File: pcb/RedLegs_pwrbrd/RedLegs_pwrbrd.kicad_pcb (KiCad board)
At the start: 2 copper layers, 25 parts, among them J1 Conn_01x02, J10 Conn_01x02, J11 Conn_01x02, J12 Conn_01x02, J2 Conn_01x02, J3 Conn_01x02, J4 Conn_01x02, J5 Conn_01x02, J6 Conn_01x02, J7 Conn_01x02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

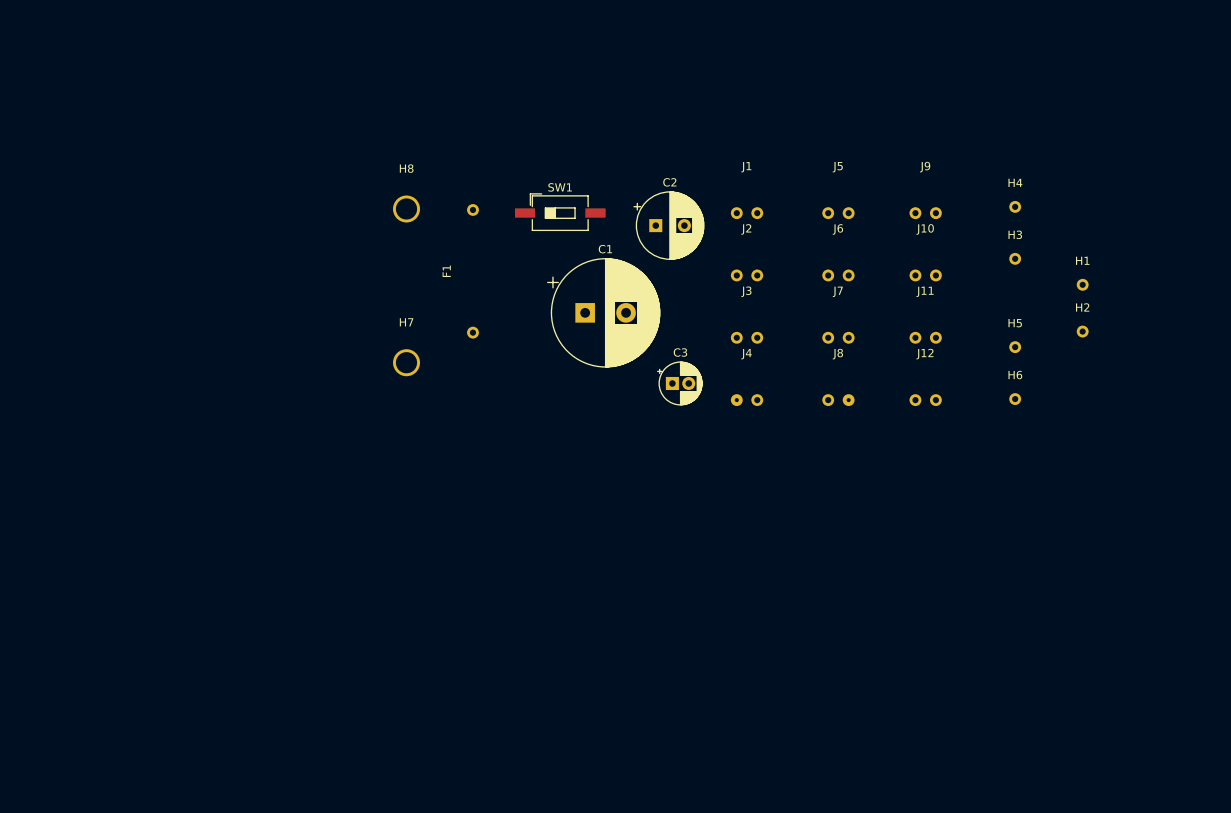
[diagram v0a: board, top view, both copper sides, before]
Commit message: Fixed power schematic, working on pcb
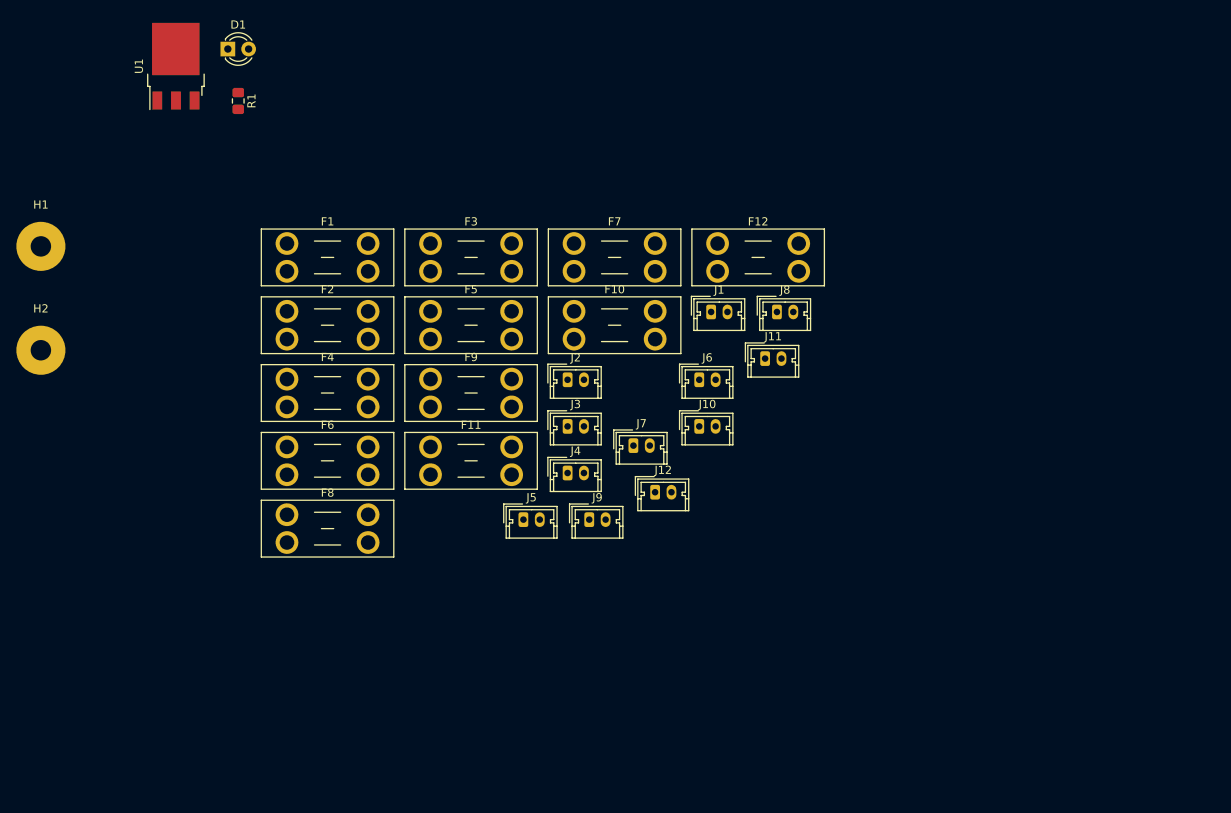
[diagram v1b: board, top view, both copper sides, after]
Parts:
- removed C1: 1000 uf, Capacitor_THT:CP_Radial_D13.0mm_P5.00mm
- removed C2: 100 uf, Capacitor_THT:CP_Radial_D8.0mm_P3.50mm
- removed C3: 10 uf, Capacitor_THT:CP_Radial_D5.0mm_P2.00mm
- removed H3, H4, H5, H6: MountingHole_Pad, MountingHole:MountingHole_2.2mm_M2_DIN965_Pad
- removed H7, H8: MountingHole_Pad, RedLegs_pwrbrd:RedLegsPwrBrdMountingHole
- removed SW1: SW_DIP_x01, Button_Switch_SMD:SW_DIP_SPSTx01_Slide_6.7x4.1mm_W8.61mm_P2.54mm_LowProfile
- added D1: LED, LED_THT:LED_D3.0mm, F.Cu at (71.1, 47.0)
- added F10: Fuse, Fuse:Fuseholder_Blade_Mini_Keystone_3568, F.Cu at (113.5, 79.1)
- added F11: Fuse, Fuse:Fuseholder_Blade_Mini_Keystone_3568, F.Cu at (95.9, 95.6)
- added F12: Fuse, Fuse:Fuseholder_Blade_Mini_Keystone_3568, F.Cu at (131.0, 70.8)
- added F2: Fuse, Fuse:Fuseholder_Blade_Mini_Keystone_3568, F.Cu at (78.3, 79.1)
- added F3: Fuse, Fuse:Fuseholder_Blade_Mini_Keystone_3568, F.Cu at (95.9, 70.8)
- added F4: Fuse, Fuse:Fuseholder_Blade_Mini_Keystone_3568, F.Cu at (78.3, 87.3)
- added F5: Fuse, Fuse:Fuseholder_Blade_Mini_Keystone_3568, F.Cu at (95.9, 79.1)
- added F6: Fuse, Fuse:Fuseholder_Blade_Mini_Keystone_3568, F.Cu at (78.3, 95.6)
- added F7: Fuse, Fuse:Fuseholder_Blade_Mini_Keystone_3568, F.Cu at (113.5, 70.8)
- added F8: Fuse, Fuse:Fuseholder_Blade_Mini_Keystone_3568, F.Cu at (78.3, 103.9)
- added F9: Fuse, Fuse:Fuseholder_Blade_Mini_Keystone_3568, F.Cu at (95.9, 87.3)
- added R1: 330, Resistor_SMD:R_0805_2012Metric_Pad1.15x1.40mm_HandSolder, F.Cu at (72.4, 53.3)
- added U1: L7805, Package_TO_SOT_SMD:TO-252-3_TabPin2, F.Cu at (64.8, 49.1)
- F1: value 30 Amps -> Fuse; footprint RedLegs_pwrbrd:RedLegsPwrBrdFuse -> Fuse:Fuseholder_Blade_Mini_Keystone_3568
- H1: value MountingHole_Pad -> Battery_Positive; footprint MountingHole:MountingHole_2.2mm_M2_DIN965_Pad -> Connector_Wire:SolderWirePad_1x01_Drill2.5mm
- H2: value MountingHole_Pad -> Battery_Ground; footprint MountingHole:MountingHole_2.2mm_M2_DIN965_Pad -> Connector_Wire:SolderWirePad_1x01_Drill2.5mm
- J1, J10, J11, J12, J2, J3, J4, J5, J6, J7, J8, J9: footprint RedLegs_pwrbrd:RedLegsPwrBrdConnector -> Connector_Molex:Molex_Micro-Latch_53253-0270_1x02_P2.00mm_Vertical
- moved H1 127.5 mm to (48.3, 71.1)
- moved H2 127.4 mm to (48.3, 83.8)
- moved J9 55.7 mm to (115.3, 104.5)
- moved J5 53.8 mm to (107.3, 104.5)
- moved J12 35.0 mm to (123.4, 101.2)
- moved J10 33.3 mm to (128.8, 93.1)
- moved J7 28.3 mm to (120.7, 95.5)
- moved J2 25.4 mm to (112.7, 87.4)
- moved J3 24.5 mm to (112.7, 93.1)
- moved J4 23.7 mm to (112.7, 98.8)
- moved F1 23.0 mm to (78.3, 70.8), turned to 0 degrees
- moved J6 21.3 mm to (128.8, 87.4)
- moved J11 19.8 mm to (136.8, 84.8)
- moved J8 13.1 mm to (138.3, 79.1)
- moved J1 12.9 mm to (130.2, 79.1)
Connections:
- net Net-(C1-Pad2) renamed GND
- F1 pad 2: Net-(F1-Pad2) -> +BATT
- H1 pad 1: Net-(C1-Pad1) -> +BATT
- J1 pad 1: Net-(C1-Pad1) -> Net-(F1-Pad1)
- J10 pad 1: Net-(C1-Pad1) -> Net-(F10-Pad1)
- J11 pad 1: Net-(C1-Pad1) -> Net-(F11-Pad1)
- J12 pad 1: Net-(C1-Pad1) -> Net-(F12-Pad1)
- J2 pad 1: Net-(C1-Pad1) -> Net-(F2-Pad1)
- J3 pad 1: Net-(C1-Pad1) -> Net-(F3-Pad1)
- J4 pad 1: Net-(C1-Pad1) -> Net-(F4-Pad1)
- J5 pad 1: Net-(C1-Pad1) -> Net-(F5-Pad1)
- J6 pad 1: Net-(C1-Pad1) -> Net-(F6-Pad1)
- J7 pad 1: Net-(C1-Pad1) -> Net-(F7-Pad1)
- J8 pad 1: Net-(C1-Pad1) -> Net-(F8-Pad1)
- J9 pad 1: Net-(C1-Pad1) -> Net-(F9-Pad1)

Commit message: Finish placement, added master fuse
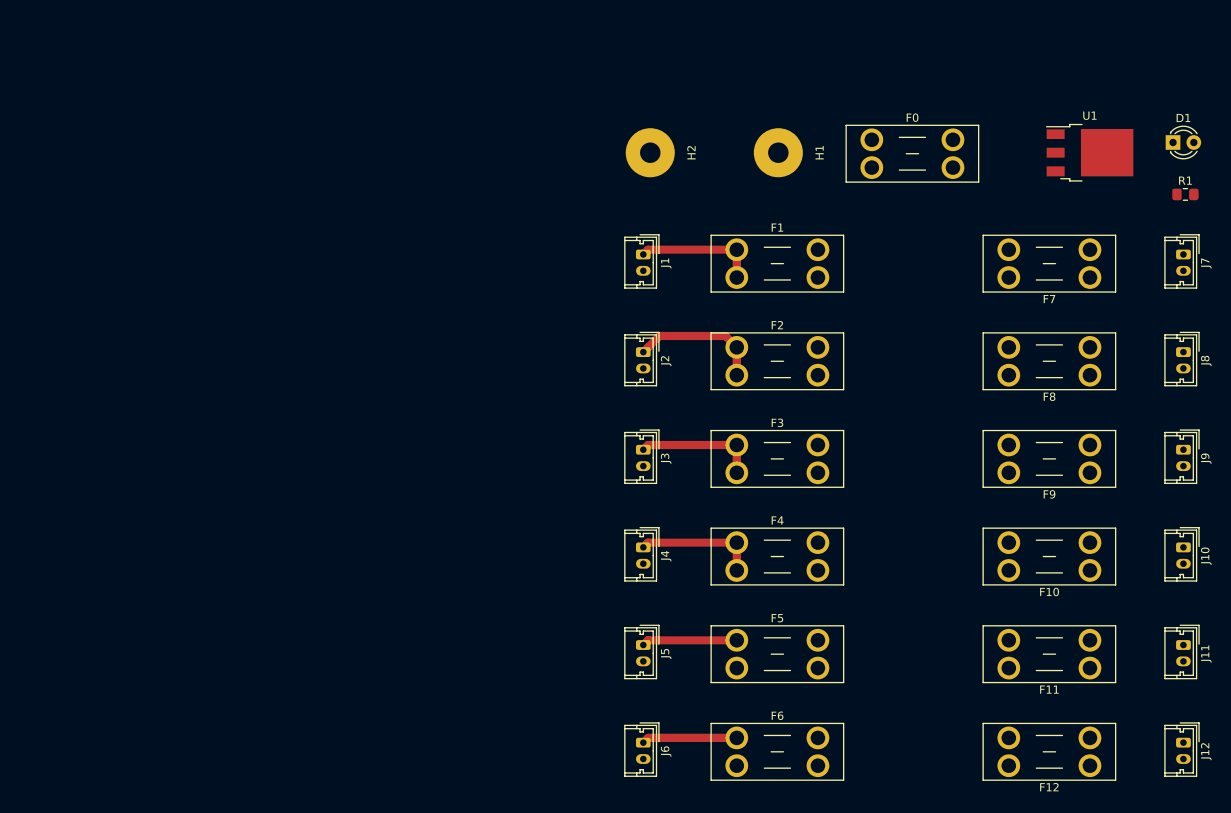
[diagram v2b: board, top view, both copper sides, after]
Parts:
- added F0: Fuse, Fuse:Fuseholder_Blade_Mini_Keystone_3568, F.Cu at (149.9, 58.1)
- moved R1 116.4 mm to (188.2, 64.8), turned to 0 degrees
- moved D1 116.1 mm to (186.7, 58.4)
- moved U1 112.3 mm to (176.5, 59.7), turned to 0 degrees
- moved F8 99.7 mm to (176.5, 86.9), turned to 180 degrees
- moved H1 90.9 mm to (138.4, 59.7), turned to 270 degrees
- moved F11 85.0 mm to (176.5, 122.7), turned to 180 degrees
- moved F9 81.4 mm to (176.5, 98.8), turned to 180 degrees
- moved F12 78.4 mm to (176.5, 134.6), turned to 180 degrees
- moved H2 78.3 mm to (122.8, 59.7), turned to 270 degrees
- moved J9 73.2 mm to (188.0, 96.0), turned to 270 degrees
- moved J12 71.5 mm to (188.0, 131.8), turned to 270 degrees
- moved J7 71.2 mm to (188.0, 72.1), turned to 270 degrees
- moved F10 70.6 mm to (176.5, 110.7), turned to 180 degrees
- moved F6 65.5 mm to (133.3, 131.2)
- moved F7 63.2 mm to (176.5, 74.9), turned to 180 degrees
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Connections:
- F1 pad 2: +BATT -> VCC
- F10 pad 2: +BATT -> VCC
- F11 pad 2: +BATT -> VCC
- F12 pad 2: +BATT -> VCC
- F2 pad 2: +BATT -> VCC
- F3 pad 2: +BATT -> VCC
- F4 pad 2: +BATT -> VCC
- F5 pad 2: +BATT -> VCC
- F6 pad 2: +BATT -> VCC
- F7 pad 2: +BATT -> VCC
- F8 pad 2: +BATT -> VCC
- F9 pad 2: +BATT -> VCC
- U1 pad 1: +BATT -> VCC
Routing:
- net Net-(F2-Pad1): track 0.00 -> 16.2 mm
- net Net-(F4-Pad1): track 0.00 -> 15.1 mm
- net Net-(F1-Pad1): track 0.00 -> 15.1 mm
- net Net-(F3-Pad1): track 0.00 -> 15.1 mm
- net Net-(F6-Pad1): track 0.00 -> 11.7 mm
- net Net-(F5-Pad1): track 0.00 -> 11.7 mm
